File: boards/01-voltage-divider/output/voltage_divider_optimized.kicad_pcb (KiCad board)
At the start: 2 copper layers, 30 x 25 mm, 4 parts, among them J1 Conn_01x02, J2 Conn_01x02

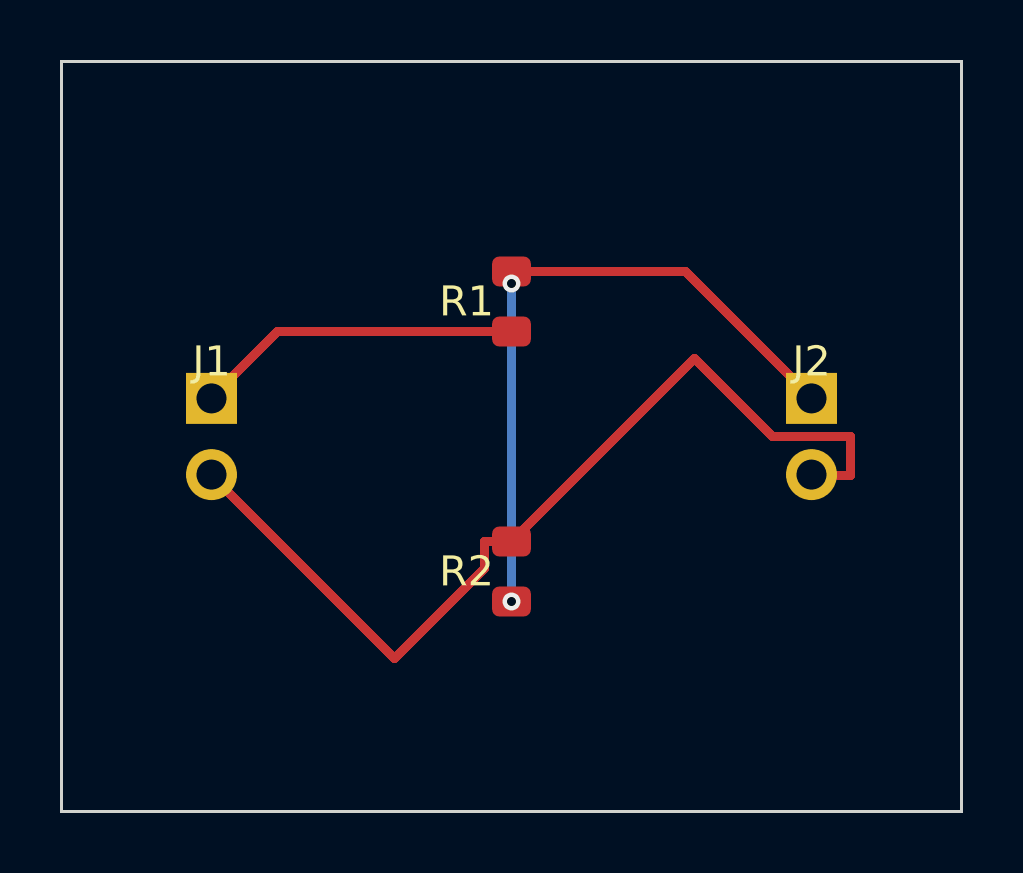
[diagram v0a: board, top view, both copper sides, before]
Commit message: refactor: Reorganize demo boards into dedicated boards/ directory
Separate complete board projects from feature examples for clarity:

boards/ (complete designs ordered by complexity):
- 01-voltage-divider: Simplest workflow validation (4 components)
- 02-charlieplex-led: Medium complexity, dense topology (14 components)
- 03-usb-joystick: Complex mixed signals, USB pairs (~20 components)
- 04-stm32-devboard: Most complex, programmatic schematic generation

examples/ (feature-specific demos):
- Retain 01-08 for schematic, BOM, DRC, placement, feedback demos
- 04-autorouter now contains only routing strategy test scripts

Also fixes:
- Rename duplicate LayoutSnapshot class to IncrementalSnapshot
- Fix router grid attribute names (cols/rows vs grid_width/grid_height)
- Create project.kct for voltage-divider example
- Update all path references in tests, benchmarks, and docs

🤖 Generated with [Claude Code](https://claude.com/claude-code)

Co-Authored-By: Claude Opus 4.5 <noreply@anthropic.com>
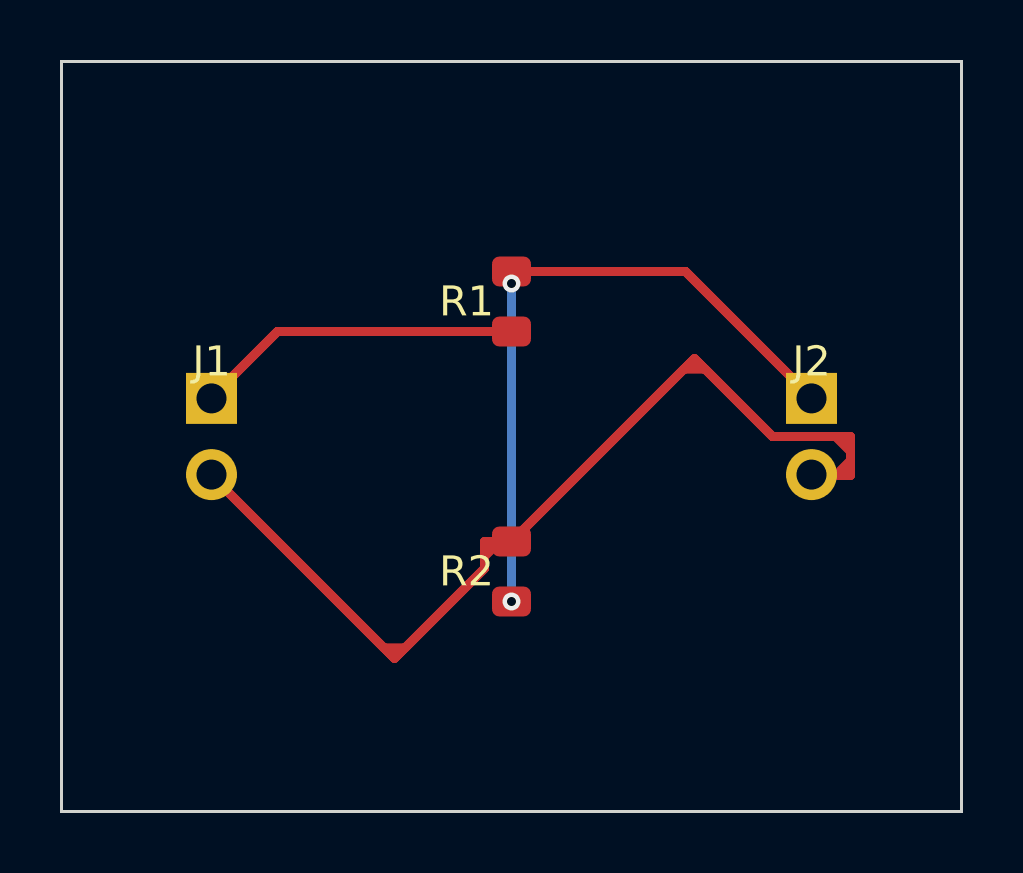
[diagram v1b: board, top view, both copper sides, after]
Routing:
- net GND: track 32.2 -> 62.5 mm
- net VOUT: track 22.8 -> 45.5 mm
- net VIN: track 10.9 -> 21.9 mm
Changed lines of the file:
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@@
+		(net 2)
+	)
+  (segment
+		(start 105.0000 113.7700)
+		(end 105.0000 113.8000)
+		(width 0.3)
+		(layer "F.Cu")
+		(net 3)
+	)
+  (segment
+		(start 105.0000 113.8000)
+		(end 110.7464 119.5464)
+		(width 0.3)
+		(layer "F.Cu")
+		(net 3)
+	)
+  (segment
+		(start 110.7464 119.5464)
+		(end 111.4536 119.5464)
+		(width 0.3)
+		(layer "F.Cu")
+		(net 3)
+	)
+  (segment
+		(start 111.4536 119.5464)
+		(end 114.1000 116.9000)
+		(width 0.3)
+		(layer "F.Cu")
+		(net 3)
+	)
+  (segment
+		(start 114.1000 116.9000)
+		(end 114.1000 116.5000)
+		(width 0.3)
+		(layer "F.Cu")
+		(net 3)
+	)
+  (segment
+		(start 114.1000 116.5000)
+		(end 114.6000 116.0000)
+		(width 0.3)
+		(layer "F.Cu")
+		(net 3)
+	)
+  (segment
+		(start 114.6000 116.0000)
+		(end 115.0000 116.0000)
+		(width 0.3)
+		(layer "F.Cu")
+		(net 3)
+	)
+  (segment
+		(start 115.0000 116.0000)
+		(end 120.7464 110.2536)
+		(width 0.3)
+		(layer "F.Cu")
+		(net 3)
+	)
+  (segment
+		(start 120.7464 110.2536)
+		(end 121.4536 110.2536)
+		(width 0.3)
+		(layer "F.Cu")
+		(net 3)
+	)
+  (segment
+		(start 121.4536 110.2536)
+		(end 123.7000 112.5000)
+		(width 0.3)
+		(layer "F.Cu")
+		(net 3)
+	)
+  (segment
+		(start 123.7000 112.5000)
+		(end 125.8000 112.5000)
+		(width 0.3)
+		(layer "F.Cu")
+		(net 3)
+	)
+  (segment
+		(start 125.8000 112.5000)
+		(end 126.3000 113.0000)
+		(width 0.3)
+		(layer "F.Cu")
+		(net 3)
+	)
+  (segment
+		(start 126.3000 113.0000)
+		(end 126.3000 113.3000)
+		(width 0.3)
+		(layer "F.Cu")
+		(net 3)
+	)
+  (segment
+		(start 126.3000 113.3000)
+		(end 125.8000 113.8000)
+		(width 0.3)
+		(layer "F.Cu")
+		(net 3)
+	)
+  (segment
+		(start 125.8000 113.8000)
+		(end 125.5000 113.8000)
+		(width 0.3)
+		(layer "F.Cu")
+		(net 3)
+	)
+  (segment
+		(start 125.0000 113.8000)
+		(end 125.0000 113.7700)
+		(width 0.3)
+		(layer "F.Cu")
+		(net 3)
+	)
+  (segment
+		(start 105.0000 111.2300)
+		(end 105.0000 111.2000)
+		(width 0.3)
+		(layer "F.Cu")
+		(net 1)
+	)
+  (segment
+		(start 105.0000 111.2000)
+		(end 107.2000 109.0000)
+		(width 0.3)
+		(layer "F.Cu")
+		(net 1)
+	)
+  (segment
+		(start 107.2000 109.0000)
+		(end 115.0000 109.0000)
+		(width 0.3)
+		(layer "F.Cu")
+		(net 1)
+	)
+  (segment
+		(start 115.0000 118.0000)
+		(end 115.0000 107.4000)
+		(width 0.3)
+		(layer "B.Cu")
+		(net 2)
+	)
+  (segment
+		(start 115.0000 107.4000)
+		(end 115.0000 107.0000)
+		(width 0.3)
+		(layer "F.Cu")
+		(net 2)
+	)
+  (segment
+		(start 115.0000 107.0000)
+		(end 115.5000 107.0000)
+		(width 0.3)
+		(layer "F.Cu")
+		(net 2)
+	)
+  (segment
+		(start 115.5000 107.0000)
+		(end 120.8000 107.0000)
+		(width 0.3)
+		(layer "F.Cu")
+		(net 2)
+	)
+  (segment
+		(start 120.8000 107.0000)
+		(end 125.0000 111.2000)
+		(width 0.3)
+		(layer "F.Cu")
+		(net 2)
+	)
+  (segment
+		(start 125.0000 111.2000)
+		(end 125.0000 111.2300)
+		(width 0.3)
+		(layer "F.Cu")
 		(net 2)
 	)
